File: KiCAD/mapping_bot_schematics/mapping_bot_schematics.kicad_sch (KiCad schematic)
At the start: 3 parts, among them M1 Motor_DC, M2 Motor_DC, U1 TB6612FNG

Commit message: Update schematics
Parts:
- added A1: Arduino_Nano_ESP32, Module:Arduino_Nano, symbol MCU_Module:Arduino_Nano_ESP32
- added BT1: Battery, symbol Device:Battery
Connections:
- net at U1.18 (GND): now also A1.29 (GND), A1.4 (GND), BT1.2 (-)
- net at U1.20 (VCC): now also A1.27 (VUSB/5V)
- net at U1.24 (VM1): now also BT1.1 (+)

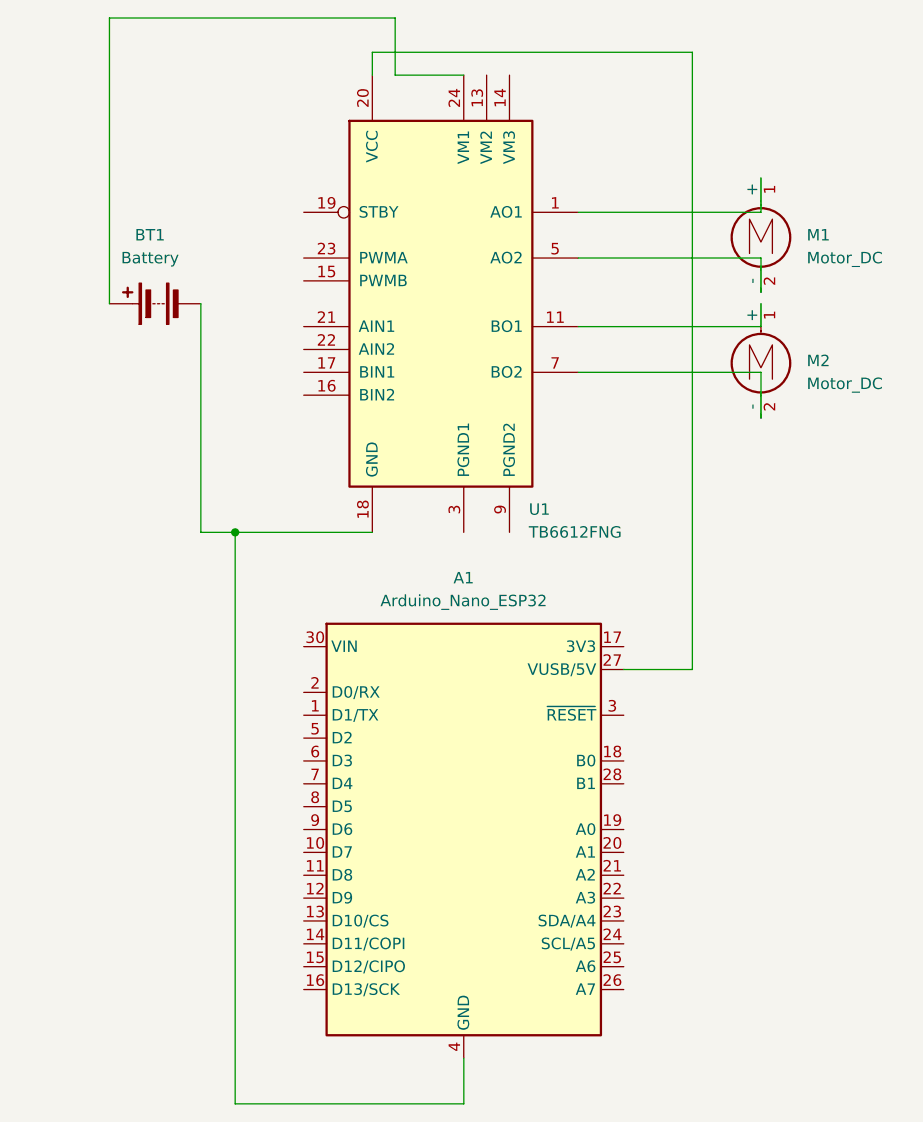
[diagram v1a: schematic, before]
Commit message: Update schematics
Basic wiring of driver and board finished
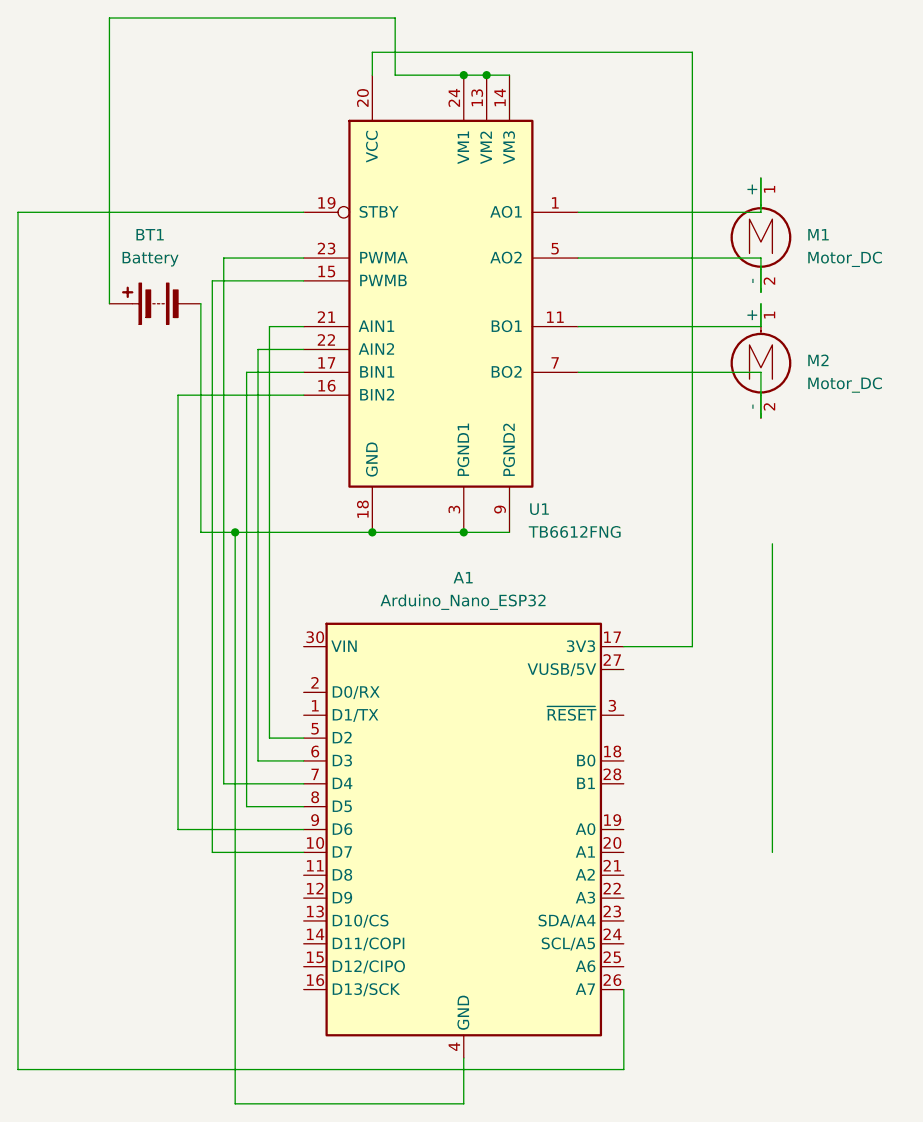
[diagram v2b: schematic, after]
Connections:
- net at A1.10 (D7): now also U1.15 (PWMB)
- net at A1.17 (3V3): now also U1.20 (VCC)
- net at A1.26 (A7): now also U1.19 (STBY)
- net at A1.27 (VUSB/5V): no longer U1.20 (VCC)
- net at A1.29 (GND), A1.4 (GND), BT1.2 (-)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: now also U1.10 (PGND2), U1.3 (PGND1), U1.4 (PGND1), U1.9 (PGND2)
- net at A1.5 (D2): now also U1.21 (AIN1)
- net at A1.6 (D3): now also U1.22 (AIN2)
- net at A1.7 (D4): now also U1.23 (PWMA)
- net at A1.8 (D5): now also U1.17 (BIN1)
- net at A1.9 (D6): now also U1.16 (BIN2)
- net at BT1.1 (+), U1.24 (VM1): now also U1.13 (VM2), U1.14 (VM3)

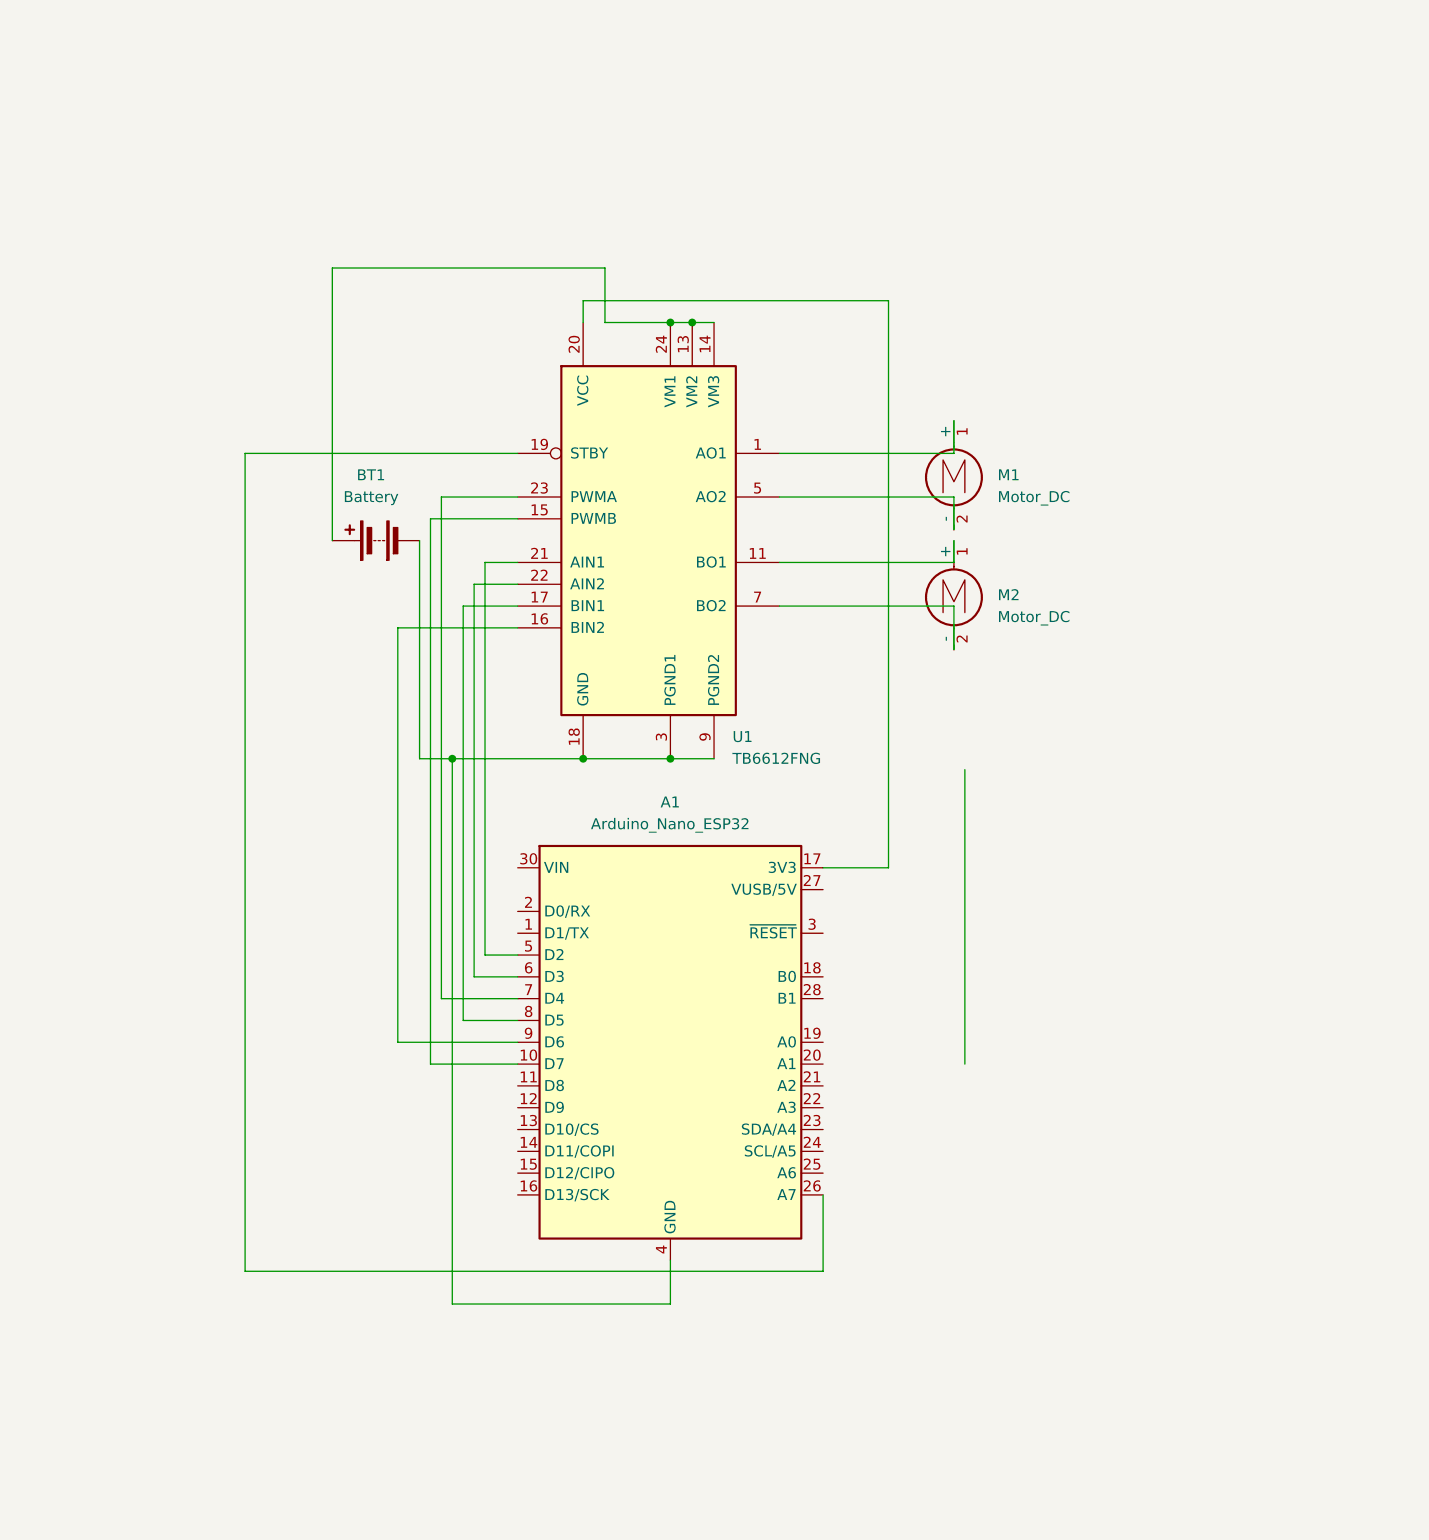
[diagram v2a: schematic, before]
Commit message: Update schematics - finish board + motor driver setup
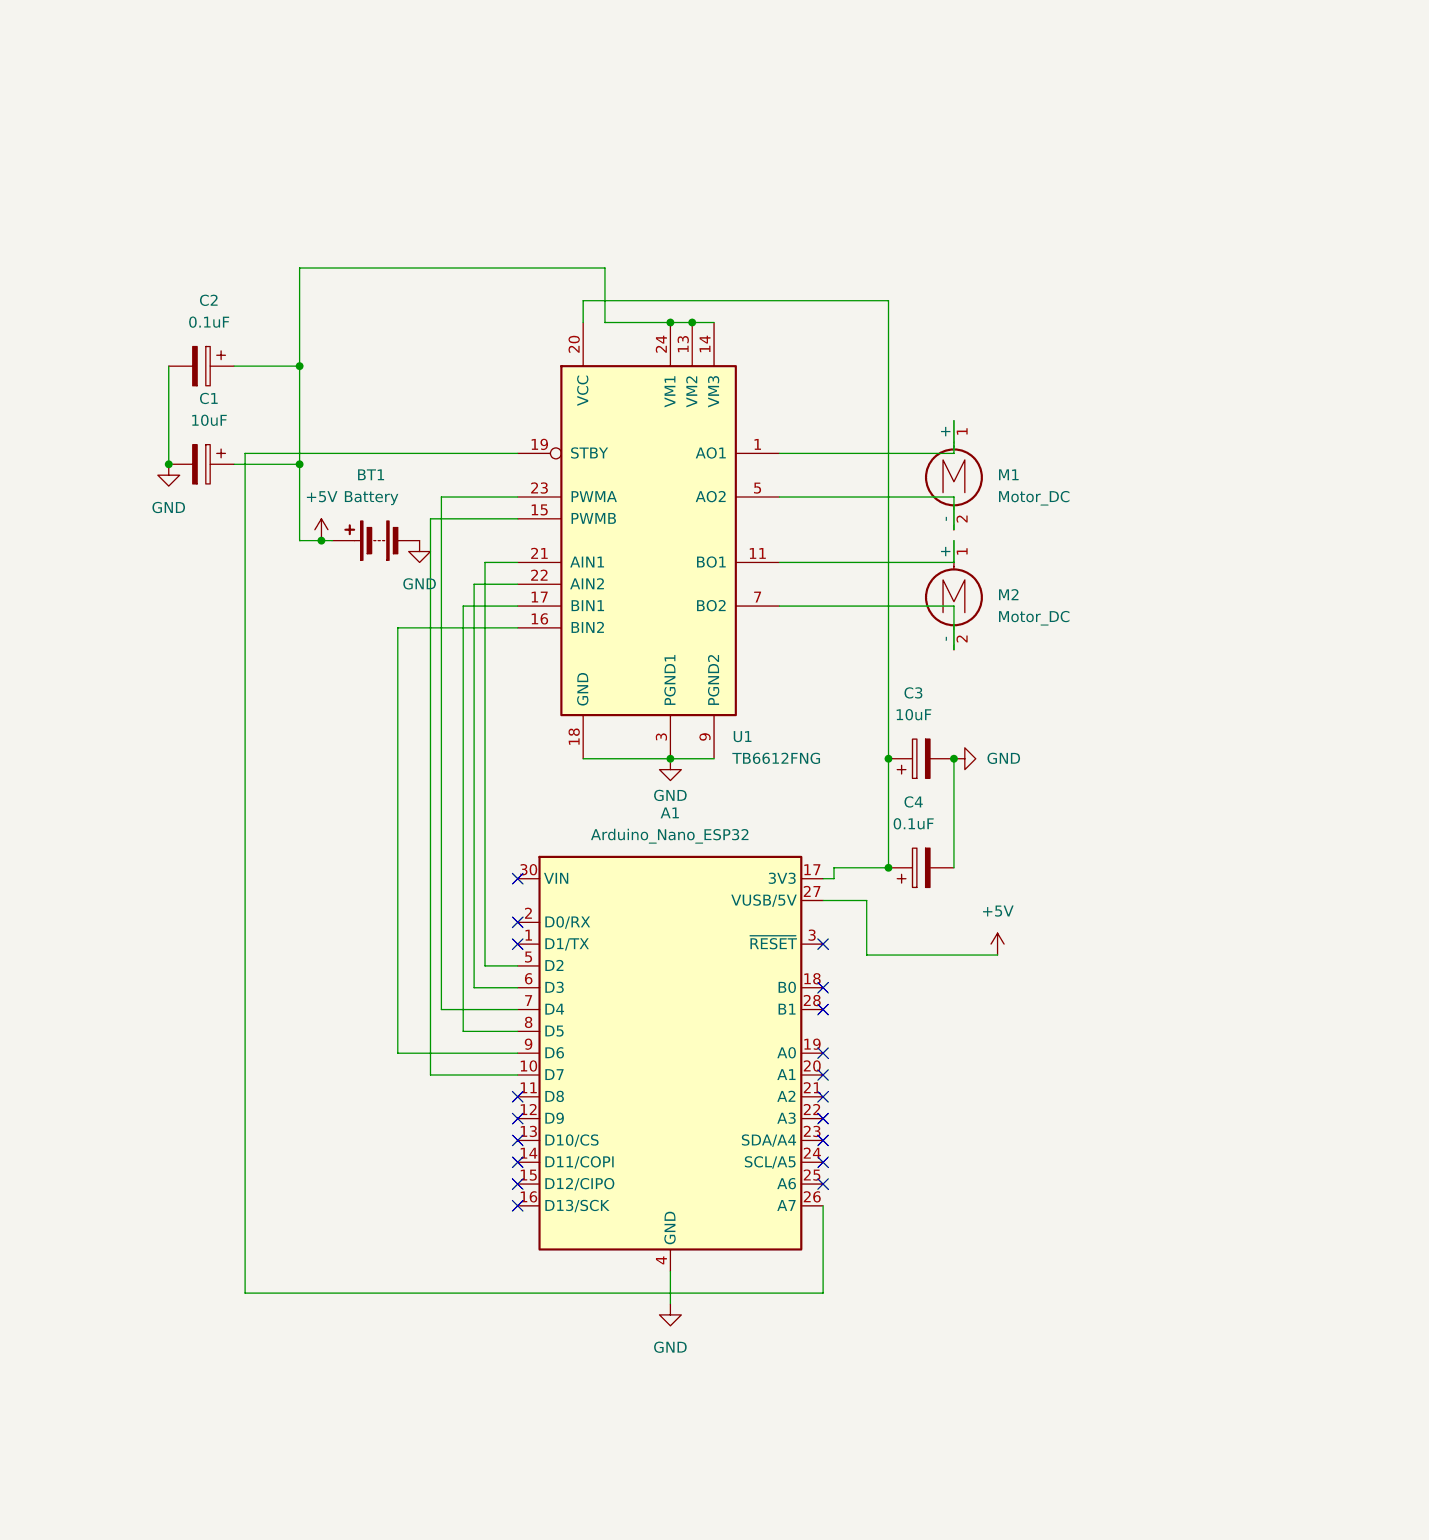
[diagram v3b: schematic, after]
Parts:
- added C1, C3: 10uF, symbol Device:C_Polarized
- added C2, C4: 0.1uF, symbol Device:C_Polarized
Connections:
- net at A1.17 (3V3), U1.20 (VCC): now also C3.1, C4.1
- net +5V: now reaches A1.27 (VUSB/5V)
- net +5V: now also BT1.1 (+), U1.13 (VM2), U1.14 (VM3), U1.24 (VM1), C1.1, C2.1
- net GND: now reaches A1.29 (GND), A1.4 (GND), BT1.2 (-), U1.10 (PGND2), U1.18 (GND), U1.3 (PGND1), U1.4 (PGND1), U1.9 (PGND2)
- net GND: now also C1.2, C2.2, C3.2, C4.2
- no-connect marks 0 -> 19
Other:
- moved on the sheet: A1

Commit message: Update schematics: change to makerboard and add distance sensor
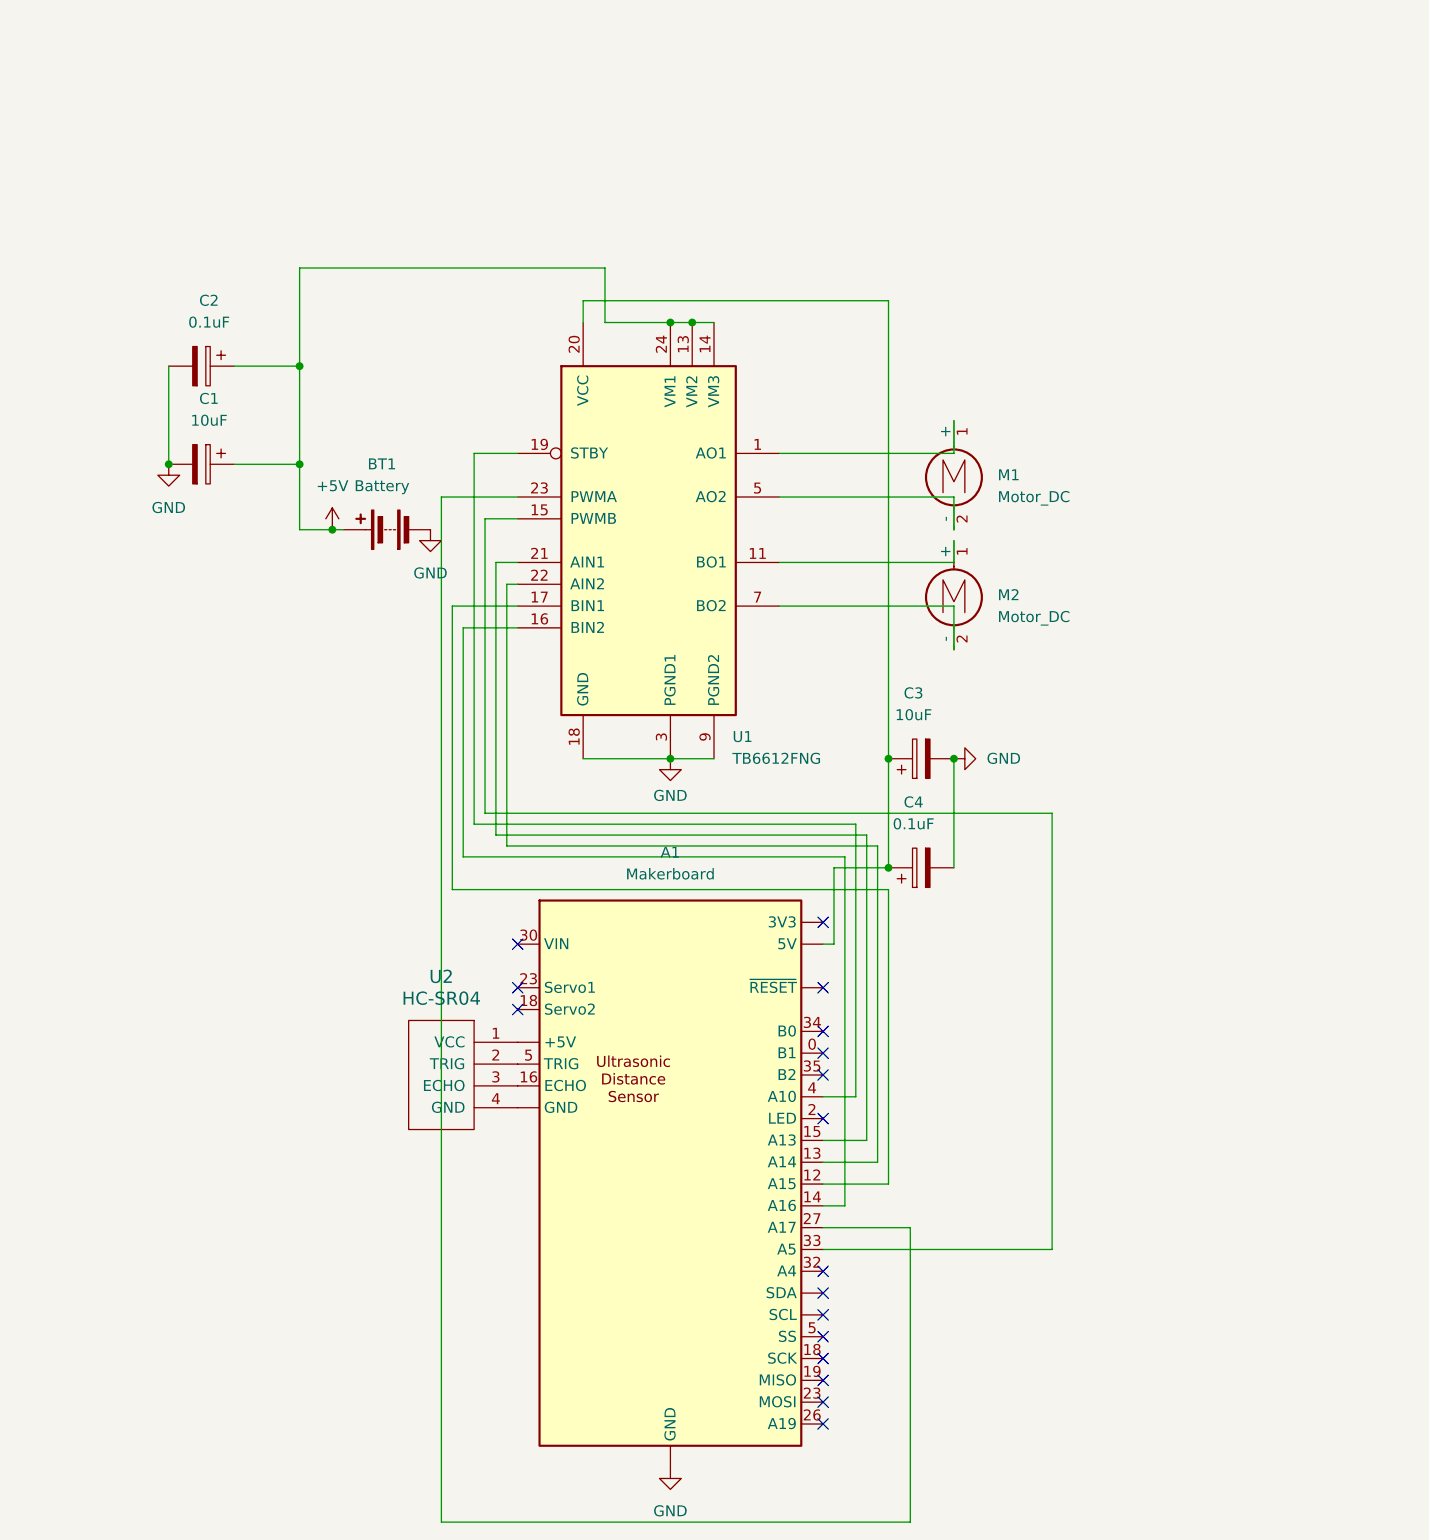
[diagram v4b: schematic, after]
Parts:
- added U2: HC-SR04, symbol HC-SR04:HC-SR04
- A1: value Arduino_Nano_ESP32 -> Makerboard; footprint Module:Arduino_Nano -> (none)
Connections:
- net +5V: no longer A1.27 (VUSB/5V)
- net GND: now also A1. (SCL); no longer A1.29 (GND), A1.4 (GND)
- net at U1.15 (PWMB): now also A1.33 (A5); no longer A1.10 (D7)
- net at A1.12 (A15): now also U1.17 (BIN1)
- net at A1.13 (A14): now also U1.22 (AIN2)
- net at A1.14 (A16): now also U1.16 (BIN2)
- net at A1.15 (A13): now also U1.21 (AIN1)
- net at A1.16 (ECHO): now also U2.3 (ECHO)
- net at C3.1, C4.1, U1.20 (VCC): now also A1. (SCL); no longer A1.17 (3V3)
- net at A1.26 (A19): no longer U1.19 (STBY)
- net at A1.5 (SS): now also U2.2 (TRIG); no longer U1.21 (AIN1)
- net at U1.23 (PWMA): now also A1.27 (A17); no longer A1.7 (D4)
- new net: A1. (SCL), U2.1 (VCC)
- new net: A1. (SCL), U2.4 (GND)
- new net: A1.4 (A10), U1.19 (STBY)
- no-connect marks 19 -> 17
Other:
- moved on the sheet: BT1
